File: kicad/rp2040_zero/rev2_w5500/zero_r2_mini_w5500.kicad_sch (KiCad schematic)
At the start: 8 parts, among them J1 jtag, J10 Debug port, J3 Dbg, J5 Debug port, J6 Debug port, J7 Conn_01x03_Pin, J8 Debug port, J9 Conn_01x03_Pin

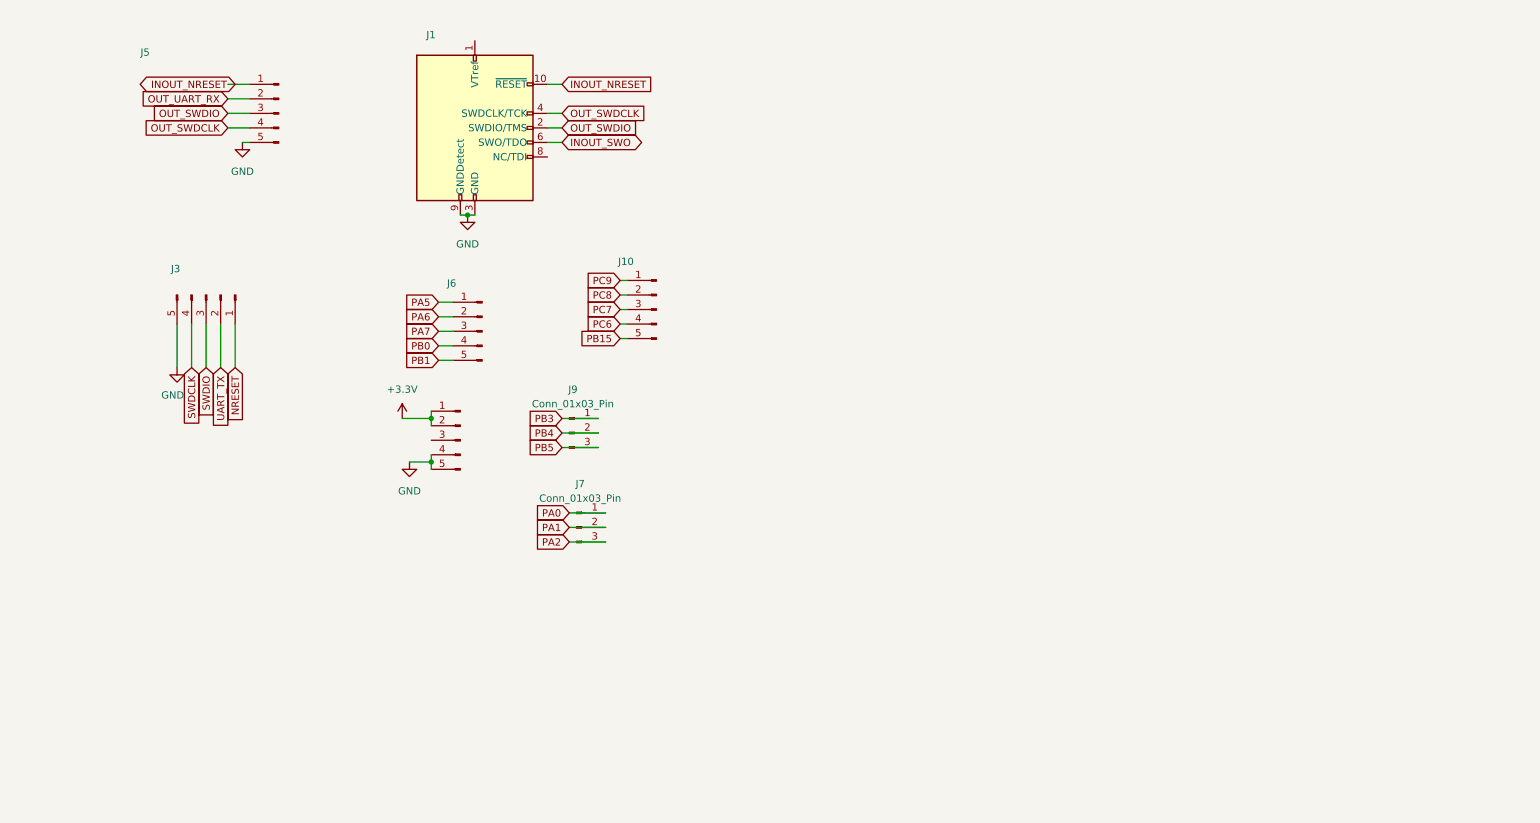
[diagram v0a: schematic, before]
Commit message: Kicad update: ch32: update pcb , add boot pin control ch32: Ground PB2 so that the internal bootloader is on USB rp_zero_mini :add mostfet to rp zero mini
general update
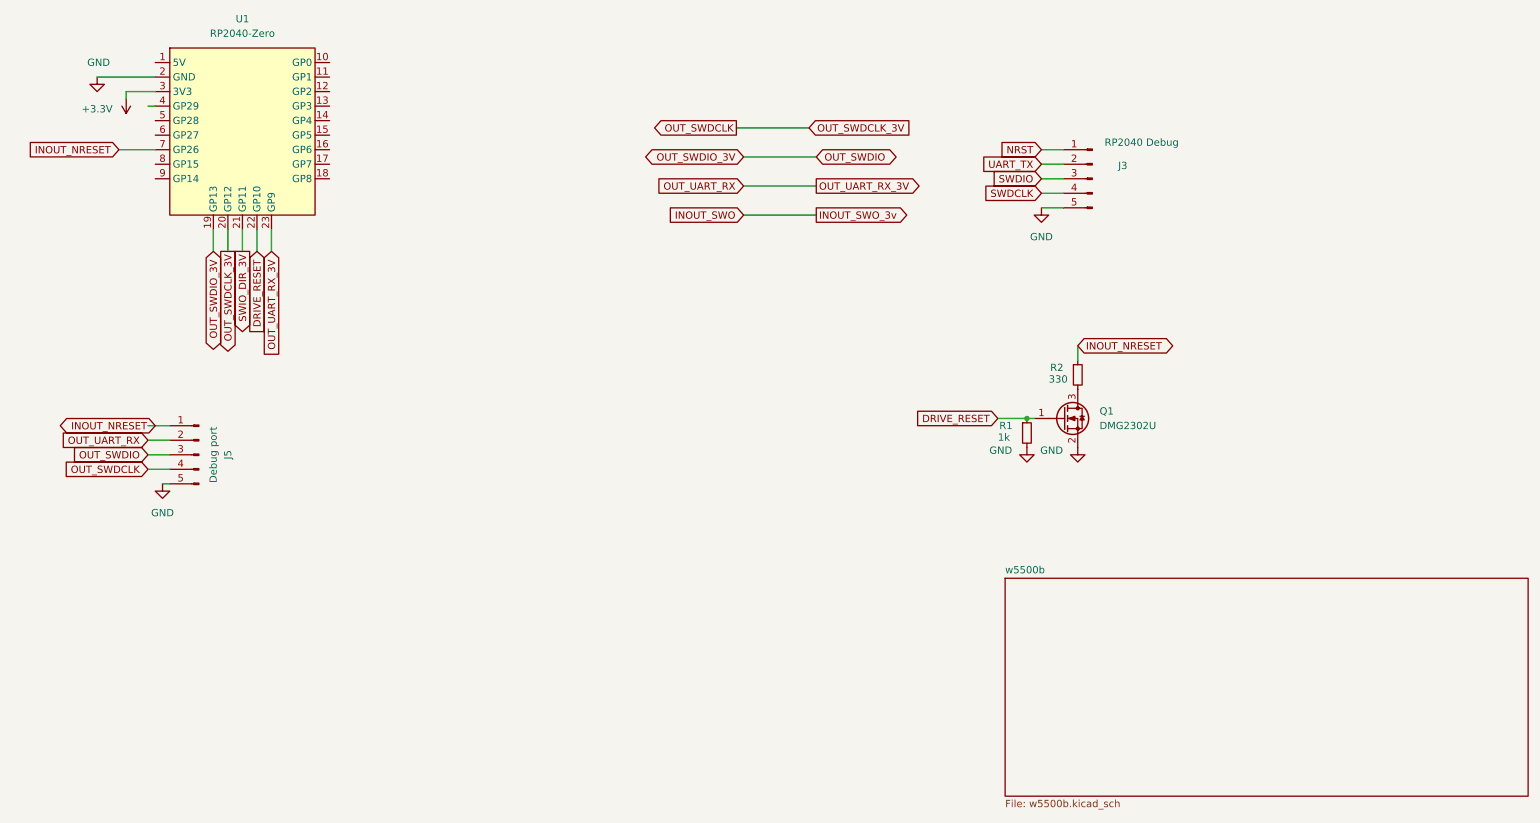
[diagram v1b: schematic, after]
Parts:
- removed J1: jtag, Connector_PinHeader_1.27mm:PinHeader_2x05_P1.27mm_Vertical_SMD, symbol Connector:Conn_ARM_JTAG_SWD_10
- removed J10, J6, J8: Debug port, Connector_PinSocket_1.27mm:PinSocket_1x05_P1.27mm_Vertical, symbol Connector:Conn_01x05_Male
- removed J7, J9: Conn_01x03_Pin, Connector_PinSocket_1.27mm:PinSocket_1x03_P1.27mm_Vertical, symbol Connector:Conn_01x03_Pin
- added Q1: DMG2302U, Package_TO_SOT_SMD:SOT-23, symbol Transistor_FET:DMG2302U
- added R1: 1k, Resistor_SMD:R_0603_1608Metric, symbol Device:R_Small
- added R2: 330, Resistor_SMD:R_0603_1608Metric, symbol Device:R_Small
- added U1: RP2040-Zero, RP2040 Carrier:RP2040 Zero, symbol CarrierZero:RP2040-Zero
- J3: value Dbg -> RP2040 Debug; footprint Connector_PinSocket_1.27mm:PinSocket_1x05_P1.27mm_Vertical -> Connector_PinHeader_1.27mm:PinHeader_1x05_P1.27mm_Vertical
- J5: footprint Connector_JST:JST_XH_B5B-XH-A_1x05_P2.50mm_Vertical -> Con5
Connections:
- net +3.3V: now also U1.3 (3V3)
- net GND: now also Q1.2 (S), R1.2, U1.2 (GND)
- net INOUT_NRESET: now also R2.1, U1.7 (GP26)
- net OUT_SWDCLK: now also U1.20 (GP12)
- net OUT_SWDIO: now also U1.19 (GP13)
- net OUT_UART_RX: now also U1.23 (GP9)
- net NRESET renamed NRST
- new net: Q1.3 (D), R2.2
- new net DRIVE_RESET: Q1.1 (G), R1.1, U1.22 (GP10)
- new net SWIO_DIR_3V: U1.21 (GP11)
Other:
- added sheet w5500b (w5500b.kicad_sch)
- title: Swindle CH32V303 -> Swindle RP2040 ZERO

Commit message: w5500 : update 1
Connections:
- net MISO: now reaches U1.10 (GP0)
- net CSn: now reaches U1.11 (GP1)
- net CLK: now reaches U1.12 (GP2)
- net MOSI: now reaches U1.13 (GP3)
- net INTn: now reaches U1.15 (GP5)
- net RSTn: now reaches U1.16 (GP6)
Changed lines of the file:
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@@
+	(wire
+		(pts
+			(xy 67.31 30.48) (xy 74.93 30.48)
+		)
+		(stroke
+			(width 0)
+			(type default)
+		)
+	)
+	(wire
+		(pts
+			(xy 67.31 22.86) (xy 73.66 22.86)
+		)
+		(stroke
+			(width 0)
+			(type default)
+		)
+	)
 	(wire
 		(pts
@@
 	(wire
 		(pts
+			(xy 67.31 38.1) (xy 74.93 38.1)
+		)
+		(stroke
+			(width 0)
+			(type default)
+		)
+	)
+	(wire
+		(pts
+			(xy 67.31 35.56) (xy 74.93 35.56)
+		)
+		(stroke
+			(width 0)
+			(type default)
+		)
+	)
+	(wire
+		(pts
 			(xy 195.58 40.64) (xy 191.77 40.64)
 		)
@@
 	(wire
 		(pts
+			(xy 67.31 27.94) (xy 74.93 27.94)
+		)
+		(stroke
+			(width 0)
+			(type default)
+		)
+	)
+	(wire
+		(pts
+			(xy 67.31 25.4) (xy 74.93 25.4)
+		)
+		(stroke
+			(width 0)
+			(type default)
+		)
+	)
+	(wire
+		(pts
 			(xy 195.58 43.18) (xy 191.77 43.18)
 		)
@@
 		)
 	)
+	(global_label "MISO"
+		(shape input)
+		(at 73.66 22.86 0)
+		(fields_autoplaced yes)
+		(effects
+			(font
+				(size 1.27 1.27)
+			)
+			(justify left)
+		)
+		(property "Intersheetrefs" "${INTERSHEET_REFS}"
+			(at 81.2414 22.86 0)
+			(hide yes)
+			(show_name no)
+			(do_not_autoplace no)
+			(effects
+				(font
+					(size 1.27 1.27)
+				)
+				(justify left)
+			)
+		)
+	)
 	(global_label "INOUT_NRESET"
 		(shape input)
@@
 				)
 				(justify right)
+			)
+		)
+	)
+	(global_label "RSTn"
+		(shape output)
+		(at 74.93 38.1 0)
+		(fields_autoplaced yes)
+		(effects
+			(font
+				(size 1.27 1.27)
+			)
+			(justify left)
+		)
+		(property "Intersheetrefs" "${INTERSHEET_REFS}"
+			(at 82.5113 38.1 0)
+			(hide yes)
+			(show_name no)
+			(do_not_autoplace no)
+			(effects
+				(font
+					(size 1.27 1.27)
+				)
+				(justify left)
 			)
 		)
@@
 		)
 	)
+	(global_label "INTn"
+		(shape input)
+		(at 74.93 35.56 0)
+		(fields_autoplaced yes)
+		(effects
+			(font
+				(size 1.27 1.27)
+			)
+			(justify left)
+		)
+		(property "Intersheetrefs" "${INTERSHEET_REFS}"
+			(at 81.9671 35.56 0)
+			(hide yes)
+			(show_name no)
+			(do_not_autoplace no)
+			(effects
+				(font
+					(size 1.27 1.27)
+				)
+				(justify left)
+			)
+		)
+	)
 	(global_label "SWDIO"
 		(shape input)
@@
 		)
 	)
+	(global_label "CSn"
+		(shape output)
+		(at 74.93 25.4 0)
+		(fields_autoplaced yes)
+		(effects
+			(font
+				(size 1.27 1.27)
+			)
+			(justify left)
+		)
+		(property "Intersheetrefs" "${INTERSHEET_REFS}"
+			(at 81.5437 25.4 0)
+			(hide yes)
+			(show_name no)
+			(do_not_autoplace no)
+			(effects
+				(font
+					(size 1.27 1.27)
+				)
+				(justify left)
+			)
+		)
+	)
 	(global_label "DRIVE_RESET"
 		(shape input)
@@
 				)
 				(justify right)
+			)
+		)
+	)
+	(global_label "MOSI"
+		(shape output)
+		(at 74.93 30.48 0)
+		(fields_autoplaced yes)
+		(effects
+			(font
+				(size 1.27 1.27)
+			)
+			(justify left)
+		)
+		(property "Intersheetrefs" "${INTERSHEET_REFS}"
+			(at 82.5114 30.48 0)
+			(hide yes)
+			(show_name no)
+			(do_not_autoplace no)
+			(effects
+				(font
+					(size 1.27 1.27)
+				)
+				(justify left)
 			)
 		)
@@
 			(hide yes)
 			(show_name no)
+			(do_not_autoplace no)
+			(effects
+				(font
+					(size 1.27 1.27)
+				)
+				(justify left)
+			)
+		)
+	)
+	(global_label "CLK"
+		(shape output)
+		(at 74.93 27.94 0)
+		(fields_autoplaced yes)
+		(effects
+			(font
+				(size 1.27 1.27)
+			)
+			(justify left)
+		)
+		(property "Intersheetrefs" "${INTERSHEET_REFS}"
+			(at 81.4833 27.94 0)
+			(hide yes)
+			(show_name no)

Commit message: preliminary W5500
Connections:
- net INTn renamed W5INTn
- net RSTn renamed W5RSTn
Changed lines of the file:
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@@
+	(wire
+		(pts
+			(xy 91.44 64.77) (xy 91.44 67.31)
+		)
+		(stroke
+			(width 0)
+			(type default)
+		)
+	)
 	(wire
 		(pts
@@
 		)
 	)
-	(global_label "RSTn"
+	(global_label "W5RSTn"
 		(shape output)
 		(at 74.93 38.1 0)
@@
 		)
 		(property "Intersheetrefs" "${INTERSHEET_REFS}"
-			(at 82.5113 38.1 0)
+			(at 85.1722 38.1 0)
 			(hide yes)
 			(show_name no)
@@
 		)
 	)
-	(global_label "INTn"
+	(global_label "W5INTn"
 		(shape input)
 		(at 74.93 35.56 0)
@@
 		)
 		(property "Intersheetrefs" "${INTERSHEET_REFS}"
-			(at 81.9671 35.56 0)
+			(at 84.628 35.56 0)
 			(hide yes)
 			(show_name no)
@@
 	(symbol
 		(lib_id "power:+3.3V")
+		(at 91.44 67.31 0)
+		(mirror x)
+		(unit 1)
+		(body_style 1)
+		(exclude_from_sim no)
+		(in_bom yes)
+		(on_board yes)
+		(in_pos_files yes)
+		(dnp no)
+		(property "Reference" "#PWR010"
+			(at 91.44 63.5 0)
+			(hide yes)
+			(show_name no)
+			(do_not_autoplace no)
+			(effects
+				(font
+					(size 1.27 1.27)
+				)
+			)
+		)
+		(property "Value" "+3.3V"
+			(at 96.52 69.088 0)
+			(show_name no)
+			(do_not_autoplace no)
+			(effects
+				(font
+					(size 1.27 1.27)
+				)
+			)
+		)
+		(property "Footprint" ""
+			(at 91.44 67.31 0)
+			(hide yes)
+			(show_name no)
+			(do_not_autoplace no)
+			(effects
+				(font
+					(size 1.27 1.27)
+				)
+			)
+		)
+		(property "Datasheet" ""
+			(at 91.44 67.31 0)
+			(hide yes)
+			(show_name no)
+			(do_not_autoplace no)
+			(effects
+				(font
+					(size 1.27 1.27)
+				)
+			)
+		)
+		(property "Description" "Power symbol creates a global label with name \"+3.3V\""
+			(at 91.44 67.31 0)
+			(hide yes)
+			(show_name no)
+			(do_not_autoplace no)
+			(effects
+				(font
+					(size 1.27 1.27)
+				)
+			)
+		)
+		(pin "1"
+		)
+		(instances
+			(project "zero_r2_mini_w5500"
+				(path "/fbe443d6-6d74-4abc-9dee-16e0160553bc"
+					(reference "#PWR010")
+					(unit 1)
+				)
+			)
+		)
+	)
+	(symbol
+		(lib_id "power:+3.3V")
 		(at 31.75 29.21 180)
 		(unit 1)
@@
 					(unit 1)
 				)
+			)
+		)
+	)
+	(symbol
+		(lib_id "W5500-EVB-Pico_V100-altium-import:3V3_BAR")
+		(at 91.44 64.77 180)
+		(unit 1)
+		(body_style 1)
+		(exclude_from_sim no)
+		(in_bom yes)
+		(on_board yes)
+		(in_pos_files yes)
+		(dnp no)
+		(property "Reference" "#PWR076"
+			(at 91.44 64.77 0)
+			(hide yes)
+			(show_name no)
+			(do_not_autoplace no)
+			(effects
+				(font
+					(size 1.27 1.27)
+				)
+			)
+		)
+		(property "Value" "3V3"
+			(at 91.44 60.96 0)
+			(show_name no)
+			(do_not_autoplace no)
+			(effects
+				(font
+					(size 1.27 1.27)
+				)
+			)
+		)
+		(property "Footprint" ""
+			(at 91.44 64.77 0)
+			(show_name no)
+			(do_not_autoplace no)
+			(effects
+				(font
+					(size 1.27 1.27)
+				)
+			)
+		)
+		(property "Datasheet" ""
+			(at 91.44 64.77 0)
+			(show_name no)
+			(do_not_autoplace no)
+			(effects
+				(font
+					(size 1.27 1.27)
+				)
+			)
+		)
+		(property "Description" ""
+			(at 91.44 64.77 0)
+			(show_name no)
+			(do_not_autoplace no)
+			(effects
+				(font
+					(size 1.27 1.27)
+				)
+			)
+		)
+		(pin ""
+		)
+		(instances
+			(project "zero_r2_mini_w5500"
+				(path "/fbe443d6-6d74-4abc-9dee-16e0160553bc"
+					(reference "#PWR076")
+					(unit 1)
+				)
